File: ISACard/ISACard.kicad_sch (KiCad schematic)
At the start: 76 parts, among them J1 Bus_ISA_8bit, J2 ICSP, J3 WIZNET, J4 SERCON, J5 Conn_01x16, Q1 2N3904, SW1 SW_Push, U1 74LS86, U11 ATmega328P-P, U12 MicroSD_SPI_CD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

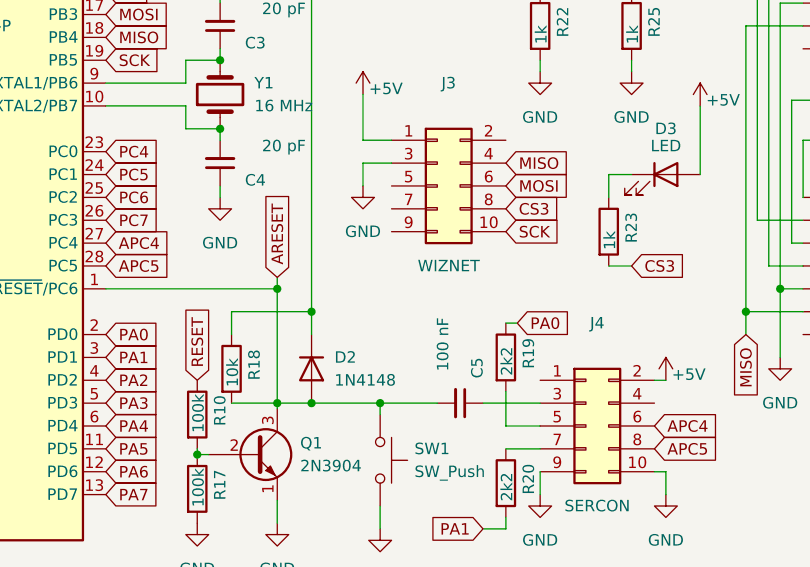
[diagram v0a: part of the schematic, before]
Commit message: Added gerber files and CS/CS2 to feature connector
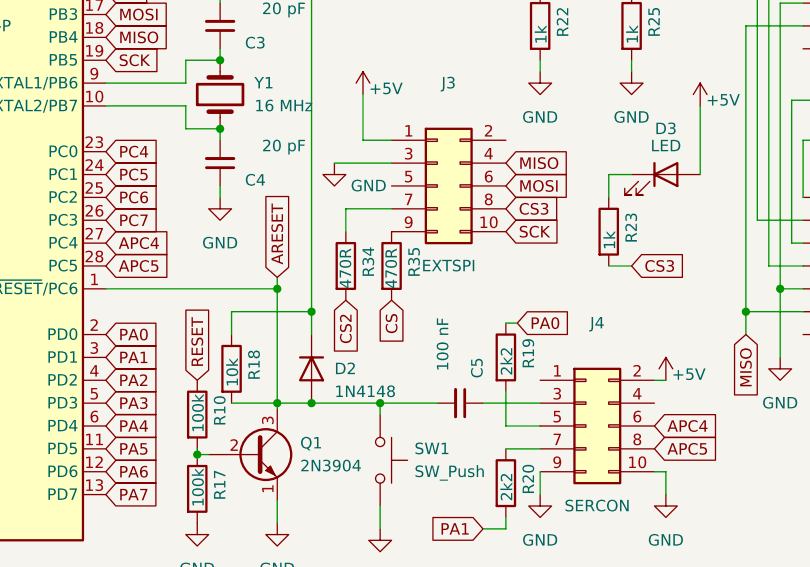
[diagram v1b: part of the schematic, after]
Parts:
- added R34, R35: 470R, Resistor_THT:R_Axial_DIN0207_L6.3mm_D2.5mm_P7.62mm_Horizontal, symbol Device:R
- J3: value WIZNET -> EXTSPI
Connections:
- net CS: now also R35.2
- net CS2: now also R34.2
- net at J3.7 (Pin_7): now also R34.1
- net at J3.9 (Pin_9): now also R35.1
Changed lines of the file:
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@@
     (stroke (width 0) (type default) (color 0 0 0 0))
   )
-  (wire (pts (xy 102.235 152.4) (xy 102.235 149.86))
-    (stroke (width 0) (type default) (color 0 0 0 0))
-  )
   (wire (pts (xy 114.3 34.29) (xy 114.3 77.47))
     (stroke (width 0) (type default) (color 0 0 0 0))
@@
     (stroke (width 0) (type default) (color 0 0 0 0))
   )
-  (wire (pts (xy 102.235 149.86) (xy 105.41 149.86))
+  (wire (pts (xy 99.06 149.86) (xy 105.41 149.86))
     (stroke (width 0) (type default) (color 0 0 0 0))
   )
@@
     (stroke (width 0) (type default) (color 0 0 0 0))
   )
+  (wire (pts (xy 100.33 154.94) (xy 105.41 154.94))
+    (stroke (width 0) (type default) (color 0 0 0 0))
+  )
   (wire (pts (xy 133.35 105.41) (xy 139.7 105.41))
     (stroke (width 0) (type default) (color 0 0 0 0))
@@
     (stroke (width 0) (type default) (color 0 0 0 0))
   )
+  (wire (pts (xy 100.33 157.48) (xy 100.33 154.94))
+    (stroke (width 0) (type default) (color 0 0 0 0))
+  )
   (wire (pts (xy 133.35 105.41) (xy 133.35 106.68))
     (stroke (width 0) (type default) (color 0 0 0 0))
@@
     )
   )
+  (global_label "CS" (shape input) (at 105.41 165.1 270) (fields_autoplaced)
+    (effects (font (size 1.27 1.27)) (justify right))
+    (property "Intersheet References" "${INTERSHEET_REFS}" (id 0) (at 105.4894 169.9926 90)
+      (effects (font (size 1.27 1.27)) (justify right) hide)
+    )
+  )
   (global_label "MEMW" (shape input) (at 35.56 58.42 180) (fields_autoplaced)
     (effects (font (size 1.27 1.27)) (justify right))
@@
     )
   )
+  (global_label "CS2" (shape input) (at 100.33 165.1 270) (fields_autoplaced)
+    (effects (font (size 1.27 1.27)) (justify right))
+    (property "Intersheet References" "${INTERSHEET_REFS}" (id 0) (at 100.4094 171.2021 90)
+      (effects (font (size 1.27 1.27)) (justify right) hide)
+    )
+  )
   (global_label "PC6" (shape input) (at 73.66 153.67 0) (fields_autoplaced)
     (effects (font (size 1.27 1.27)) (justify left))
@@
   )
   (symbol (lib_id "Device:D") (at 96.52 172.72 270) (unit 1)
-    (in_bom yes) (on_board yes) (fields_autoplaced)
-    (property "Reference" "D2" (id 0) (at 99.06 171.4499 90)
+    (in_bom yes) (on_board yes)
+    (property "Reference" "D2" (id 0) (at 99.06 172.72 90)
       (effects (font (size 1.27 1.27)) (justify left))
     )
-    (property "Value" "1N4148" (id 1) (at 99.06 173.9899 90)
+    (property "Value" "1N4148" (id 1) (at 99.06 175.26 90)
       (effects (font (size 1.27 1.27)) (justify left))
     )
@@
     (pin "1")
   )
+  (symbol (lib_id "Device:R") (at 105.41 161.29 0) (unit 1)
+    (in_bom yes) (on_board yes)
+    (property "Reference" "R35" (id 0) (at 107.95 162.56 90)
+      (effects (font (size 1.27 1.27)) (justify left))
+    )
+    (property "Value" "470R" (id 1) (at 105.41 163.83 90)
+      (effects (font (size 1.27 1.27)) (justify left))
+    )
+    (property "Footprint" "Resistor_THT:R_Axial_DIN0207_L6.3mm_D2.5mm_P7.62mm_Horizontal" (id 2) (at 103.632 161.29 90)
+      (effects (font (size 1.27 1.27)) hide)
+    )
+    (property "Datasheet" "~" (id 3) (at 105.41 161.29 0)
+      (effects (font (size 1.27 1.27)) hide)
+    )
+    (pin "1")
+    (pin "2")
+  )
   (symbol (lib_id "Device:R") (at 132.08 134.62 0) (unit 1)
     (in_bom yes) (on_board yes)
@@
     (pin "2")
   )
+  (symbol (lib_id "Device:R") (at 100.33 161.29 0) (unit 1)
+    (in_bom yes) (on_board yes)
+    (property "Reference" "R34" (id 0) (at 102.87 162.56 90)
+      (effects (font (size 1.27 1.27)) (justify left))
+    )
+    (property "Value" "470R" (id 1) (at 100.33 163.83 90)
+      (effects (font (size 1.27 1.27)) (justify left))
+    )
+    (property "Footprint" "Resistor_THT:R_Axial_DIN0207_L6.3mm_D2.5mm_P7.62mm_Horizontal" (id 2) (at 98.552 161.29 90)
+      (effects (font (size 1.27 1.27)) hide)
+    )
+    (property "Datasheet" "~" (id 3) (at 100.33 161.29 0)
+      (effects (font (size 1.27 1.27)) hide)
+    )
+    (pin "1")
+    (pin "2")
+  )
   (symbol (lib_id "Device:R") (at 118.11 185.42 0) (unit 1)
     (in_bom yes) (on_board yes)
@@
     (in_bom yes) (on_board yes)
     (property "Reference" "J3" (id 0) (at 111.76 140.97 0))
-    (property "Value" "WIZNET" (id 1) (at 111.76 161.29 0))
+    (property "Value" "EXTSPI" (id 1) (at 111.76 161.29 0))
     (property "Footprint" "Connector_PinHeader_2.54mm:PinHeader_2x05_P2.54mm_Vertical" (id 2) (at 110.49 152.4 0)
       (effects (font (size 1.27 1.27)) hide)
@@
     (pin "3")
   )
-  (symbol (lib_id "power:GND") (at 102.235 152.4 0) (unit 1)
-    (in_bom yes) (on_board yes) (fields_autoplaced)
-    (property "Reference" "#PWR0147" (id 0) (at 102.235 158.75 0)
+  (symbol (lib_id "power:GND") (at 99.06 149.86 0) (unit 1)
+    (in_bom yes) (on_board yes)
+    (property "Reference" "#PWR0147" (id 0) (at 99.06 156.21 0)
       (effects (font (size 1.27 1.27)) hide)
     )
-    (property "Value" "GND" (id 1) (at 102.235 157.48 0))
-    (property "Footprint" "" (id 2) (at 102.235 152.4 0)
+    (property "Value" "GND" (id 1) (at 102.87 152.4 0))
+    (property "Footprint" "" (id 2) (at 99.06 149.86 0)
       (effects (font (size 1.27 1.27)) hide)
     )
-    (property "Datasheet" "" (id 3) (at 102.235 152.4 0)
+    (property "Datasheet" "" (id 3) (at 99.06 149.86 0)
       (effects (font (size 1.27 1.27)) hide)
     )
@@
       (reference "#PWR0120") (unit 1) (value "GND") (footprint "")
     )
-    (path "/c9673afe-6a47-4001-a17b-47c886543b3d/3abdaf07-bb8e-44ac-a599-c3c3fb1b5d9c"
-      (reference "#PWR0121") (unit 1) (value "+5V") (footprint "")
-    )
     (path "/55acaa97-7fa9-4583-b39f-11cc909a1654"
       (reference "#PWR0122") (unit 1) (value "+5V") (footprint "")
@@
     )
     (path "/8d73aa48-f21a-42a2-97b4-044916c065b9"
-      (reference "J3") (unit 1) (value "WIZNET") (footprint "Connector_PinHeader_2.54mm:PinHeader_2x05_P2.54mm_Vertical")
+      (reference "J3") (unit 1) (value "EXTSPI") (footprint "Connector_PinHeader_2.54mm:PinHeader_2x05_P2.54mm_Vertical")
     )
     (path "/09fcf200-de96-4f41-9aa1-5e72798da4f5"
@@
       (reference "R33") (unit 1) (value "10k") (footprint "Resistor_THT:R_Axial_DIN0207_L6.3mm_D2.5mm_P7.62mm_Horizontal")
     )
+    (path "/838bdca2-c766-4985-8e01-dddd310da0af"
+      (reference "R34") (unit 1) (value "470R") (footprint "Resistor_THT:R_Axial_DIN0207_L6.3mm_D2.5mm_P7.62mm_Horizontal")
+    )
+    (path "/3ae69249-8361-4c51-b93e-32198a504a11"
+      (reference "R35") (unit 1) (value "470R") (footprint "Resistor_THT:R_Axial_DIN0207_L6.3mm_D2.5mm_P7.62mm_Horizontal")
+    )
     (path "/96797394-f9c8-4c13-b280-891904ccab0d"

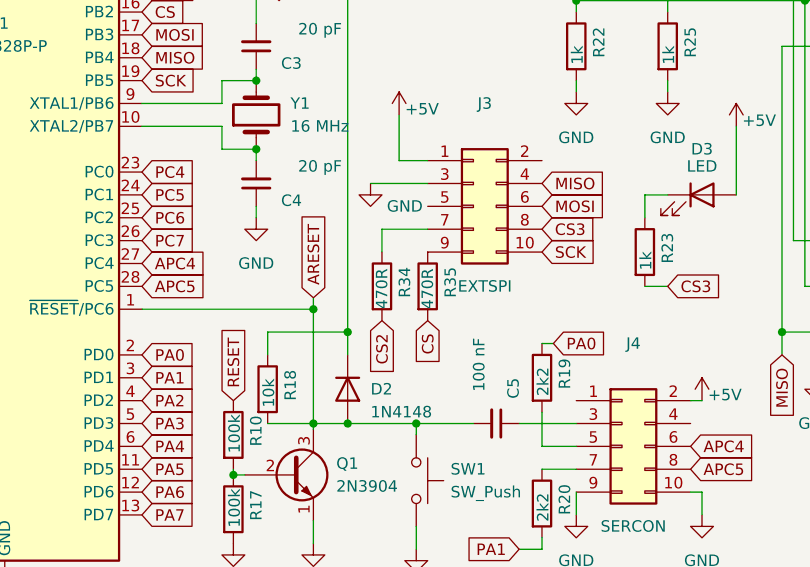
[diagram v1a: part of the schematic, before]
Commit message: Added external SD card board
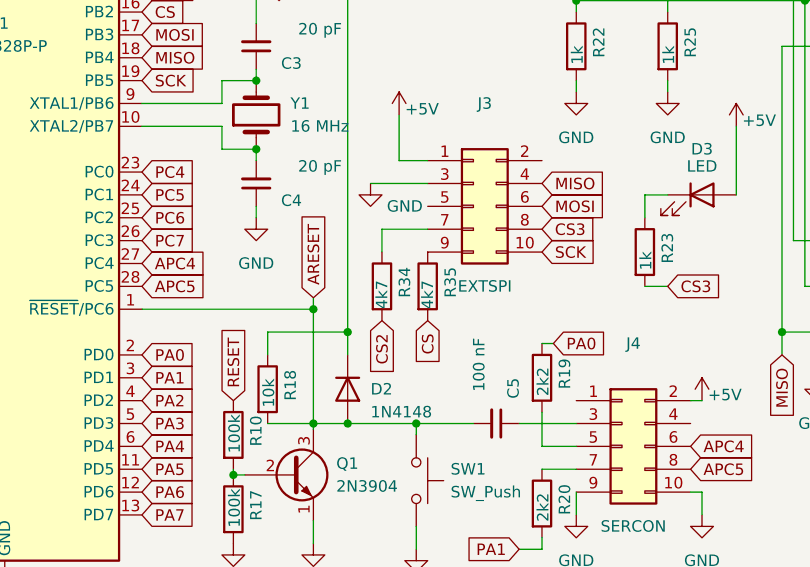
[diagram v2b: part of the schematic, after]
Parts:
- R34, R35: value 470R -> 4k7
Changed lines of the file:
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@@
       (effects (font (size 1.27 1.27)) (justify left))
     )
-    (property "Value" "470R" (id 1) (at 105.41 163.83 90)
+    (property "Value" "4k7" (id 1) (at 105.41 163.83 90)
       (effects (font (size 1.27 1.27)) (justify left))
     )
@@
       (effects (font (size 1.27 1.27)) (justify left))
     )
-    (property "Value" "470R" (id 1) (at 100.33 163.83 90)
+    (property "Value" "4k7" (id 1) (at 100.33 163.83 90)
       (effects (font (size 1.27 1.27)) (justify left))
     )
@@
     )
     (path "/838bdca2-c766-4985-8e01-dddd310da0af"
-      (reference "R34") (unit 1) (value "470R") (footprint "Resistor_THT:R_Axial_DIN0207_L6.3mm_D2.5mm_P7.62mm_Horizontal")
+      (reference "R34") (unit 1) (value "4k7") (footprint "Resistor_THT:R_Axial_DIN0207_L6.3mm_D2.5mm_P7.62mm_Horizontal")
     )
     (path "/3ae69249-8361-4c51-b93e-32198a504a11"
-      (reference "R35") (unit 1) (value "470R") (footprint "Resistor_THT:R_Axial_DIN0207_L6.3mm_D2.5mm_P7.62mm_Horizontal")
+      (reference "R35") (unit 1) (value "4k7") (footprint "Resistor_THT:R_Axial_DIN0207_L6.3mm_D2.5mm_P7.62mm_Horizontal")
     )
     (path "/96797394-f9c8-4c13-b280-891904ccab0d"

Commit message: Moved around some traces
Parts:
- R10: footprint Resistor_THT:R_Axial_DIN0207_L6.3mm_D2.5mm_P7.62mm_Horizontal -> Resistor_THT:R_Axial_DIN0207_L6.3mm_D2.5mm_P10.16mm_Horizontal
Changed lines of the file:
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@@
       (effects (font (size 1.27 1.27)) (justify left))
     )
-    (property "Footprint" "Resistor_THT:R_Axial_DIN0207_L6.3mm_D2.5mm_P7.62mm_Horizontal" (id 2) (at 82.042 177.8 90)
+    (property "Footprint" "Resistor_THT:R_Axial_DIN0207_L6.3mm_D2.5mm_P10.16mm_Horizontal" (id 2) (at 82.042 177.8 90)
       (effects (font (size 1.27 1.27)) hide)
     )
@@
     )
     (path "/a9ec56ff-b7ce-405e-969d-1dbeddd89d33"
-      (reference "R10") (unit 1) (value "100k") (footprint "Resistor_THT:R_Axial_DIN0207_L6.3mm_D2.5mm_P7.62mm_Horizontal")
+      (reference "R10") (unit 1) (value "100k") (footprint "Resistor_THT:R_Axial_DIN0207_L6.3mm_D2.5mm_P10.16mm_Horizontal")
     )
     (path "/c9673afe-6a47-4001-a17b-47c886543b3d/3d9abe83-970d-47f4-928f-b4e095fafd1c"
